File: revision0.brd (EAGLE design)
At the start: 80 x 80 mm, 92 parts, among them IC1 MSP430FR698X(1)80-PIN_PN, IC3 FT232RL

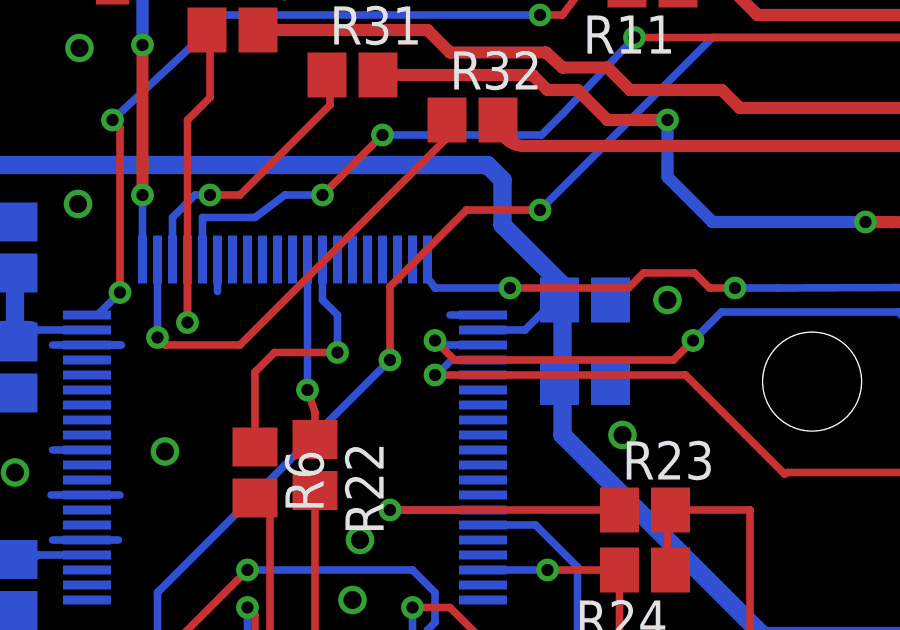
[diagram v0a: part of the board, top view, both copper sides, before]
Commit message: Turn on polygon thermals and fix one GND wire
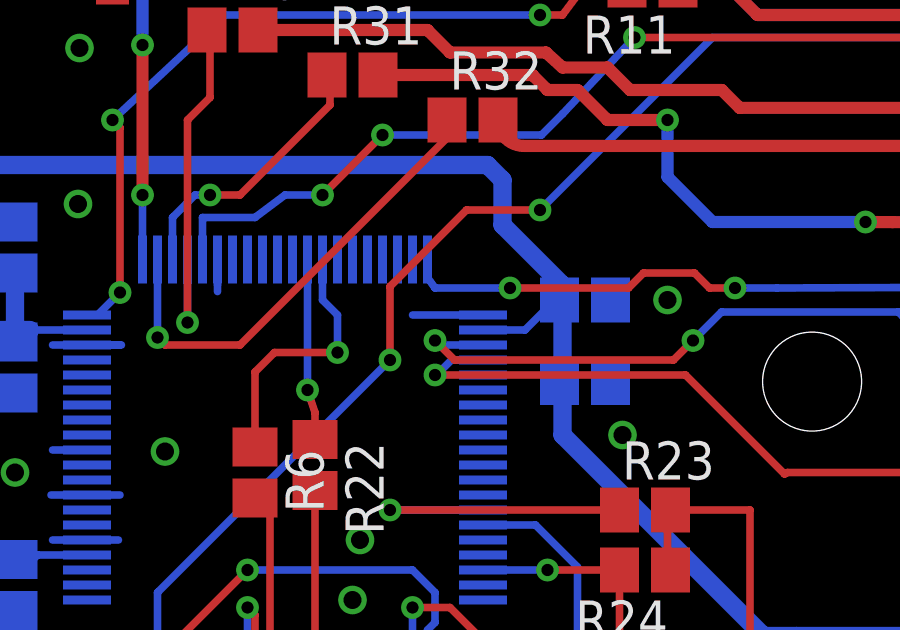
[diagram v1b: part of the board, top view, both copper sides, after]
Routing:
- net GND: track 39.8 -> 41.1 mm
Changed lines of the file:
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@@
 <wire x1="28" y1="71.075" x2="28" y2="71" width="0.4064" layer="1"/>
 <via x="28" y="71" extent="1-16" drill="0.4064"/>
-<polygon width="0.4064" layer="1" thermals="no">
+<polygon width="0.4064" layer="1">
 <vertex x="0.25" y="79.75"/>
 <vertex x="79.75" y="79.75"/>
@@
 <via x="9.25" y="77" extent="1-16" drill="0.6"/>
 <via x="11.75" y="70.75" extent="1-16" drill="0.6"/>
-<polygon width="0.4064" layer="16" thermals="no">
+<polygon width="0.4064" layer="16">
 <vertex x="0.25" y="79.75"/>
 <vertex x="79.75" y="79.75"/>
@@
 <wire x1="33.5" y1="8.5" x2="33.5" y2="11.25" width="0.6096" layer="16"/>
 <wire x1="33.5" y1="11.25" x2="37.5" y2="15.25" width="0.6096" layer="16"/>
-<wire x1="19.5" y1="52" x2="18.25" y2="52" width="0.254" layer="16"/>
+<wire x1="19.5" y1="52" x2="19.35" y2="52" width="0.254" layer="16"/>
 <wire x1="6.25" y1="46" x2="7.25" y2="46" width="0.254" layer="16"/>
 <wire x1="6.15" y1="44.5" x2="7.2" y2="44.5" width="0.254" layer="16"/>
@@
 <via x="8.2" y="68.7" extent="1-16" drill="0.6"/>
 <via x="5.9" y="60.9" extent="1-16" drill="0.6"/>
+<wire x1="19.35" y1="52" x2="17" y2="52" width="0.254" layer="16"/>
 </signal>
 <signal name="GPS-WAKEUP">

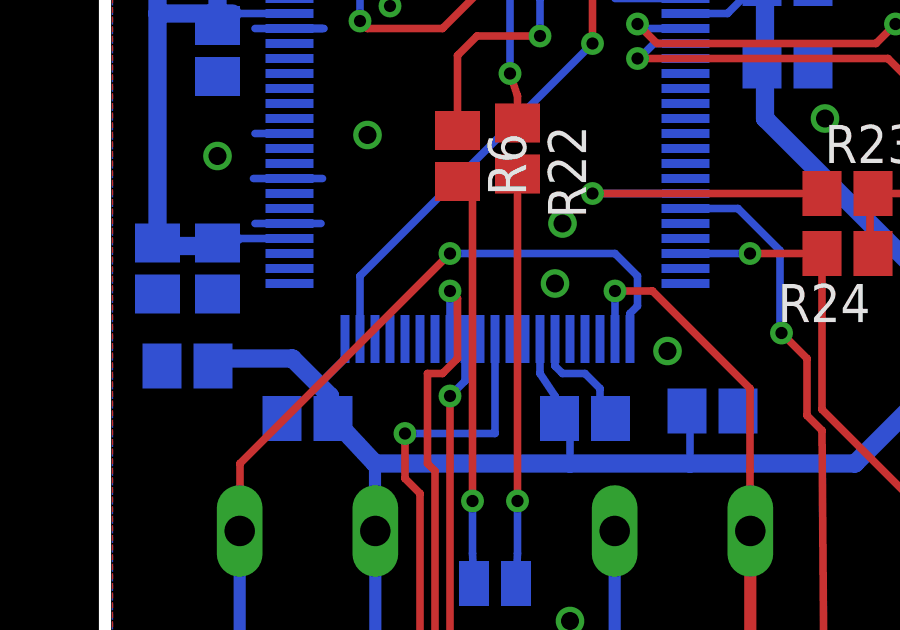
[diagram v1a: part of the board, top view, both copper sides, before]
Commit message: Move GPS-TIMEPULSE sig to interrupt capable input (P2.1)
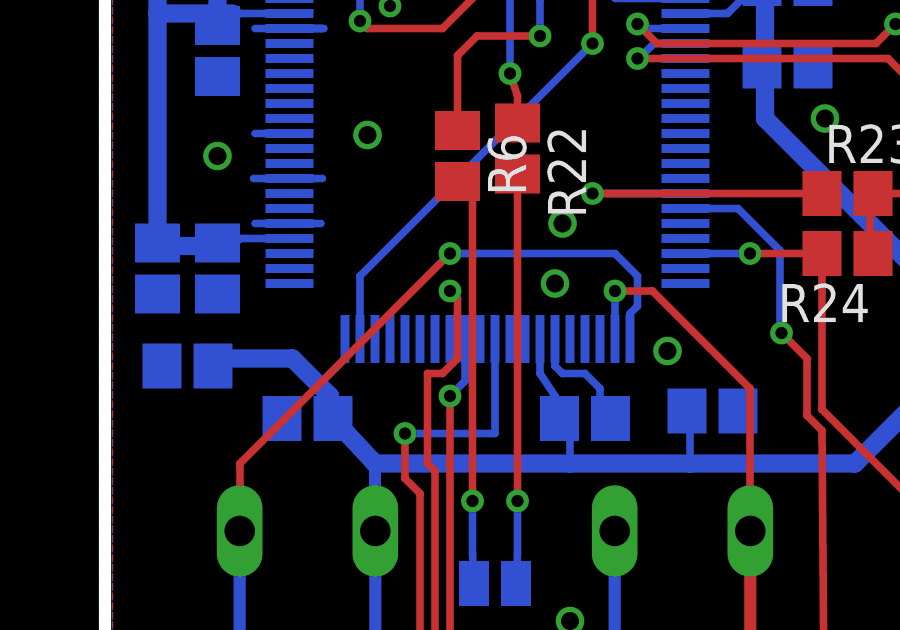
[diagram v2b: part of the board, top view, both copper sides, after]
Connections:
- net GPS-TIMEPULSE: now also IC1.40; no longer IC1.53
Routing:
- net GPS-TIMEPULSE: track 33.2 -> 31.6 mm
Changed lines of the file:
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@@
 <layer number="21" name="tPlace" color="7" fill="1" visible="no" active="yes"/>
 <layer number="22" name="bPlace" color="7" fill="1" visible="no" active="yes"/>
-<layer number="23" name="tOrigins" color="15" fill="1" visible="no" active="yes"/>
-<layer number="24" name="bOrigins" color="15" fill="1" visible="no" active="yes"/>
+<layer number="23" name="tOrigins" color="15" fill="1" visible="yes" active="yes"/>
+<layer number="24" name="bOrigins" color="15" fill="1" visible="yes" active="yes"/>
 <layer number="25" name="tNames" color="7" fill="1" visible="no" active="yes"/>
 <layer number="26" name="bNames" color="7" fill="1" visible="no" active="yes"/>
@@
 <signal name="GPS-TIMEPULSE">
 <contactref element="R28" pad="1"/>
-<contactref element="IC1" pad="53"/>
-<wire x1="11.5" y1="40.65" x2="11.5" y2="42.25" width="0.254" layer="16"/>
 <via x="11.5" y="42.25" extent="1-16" drill="0.4064"/>
 <wire x1="11.75" y1="40" x2="11.25" y2="39.5" width="0.254" layer="1"/>
@@
 <via x="16.5" y="18.95" extent="1-16" drill="0.4064"/>
 <wire x1="16.5" y1="18.95" x2="16.5" y2="13.85" width="0.254" layer="16"/>
+<contactref element="IC1" pad="40"/>
+<wire x1="11.75" y1="42" x2="19.35" y2="42.5" width="0" layer="19" extent="1-16"/>
 </signal>
 <signal name="N$3">

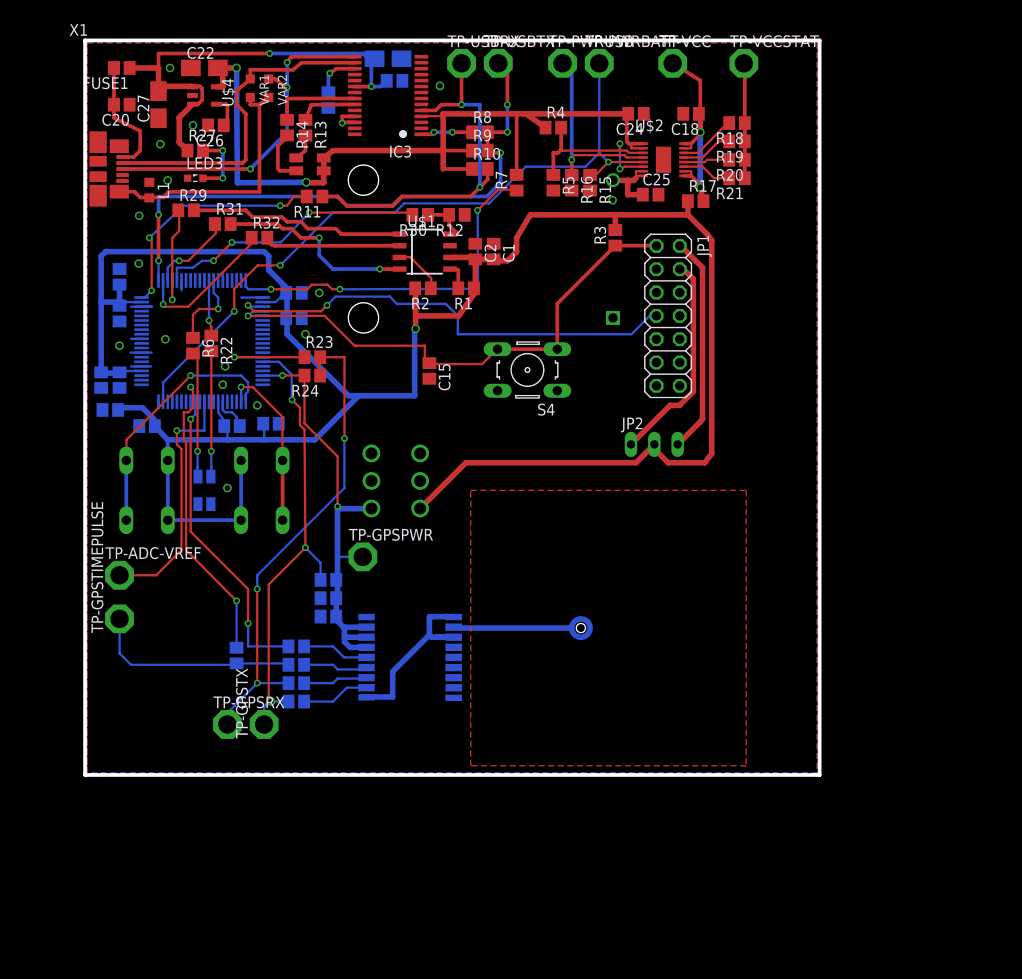
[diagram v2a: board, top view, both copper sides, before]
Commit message: Redesign a lot GPS RF part, CPU pins
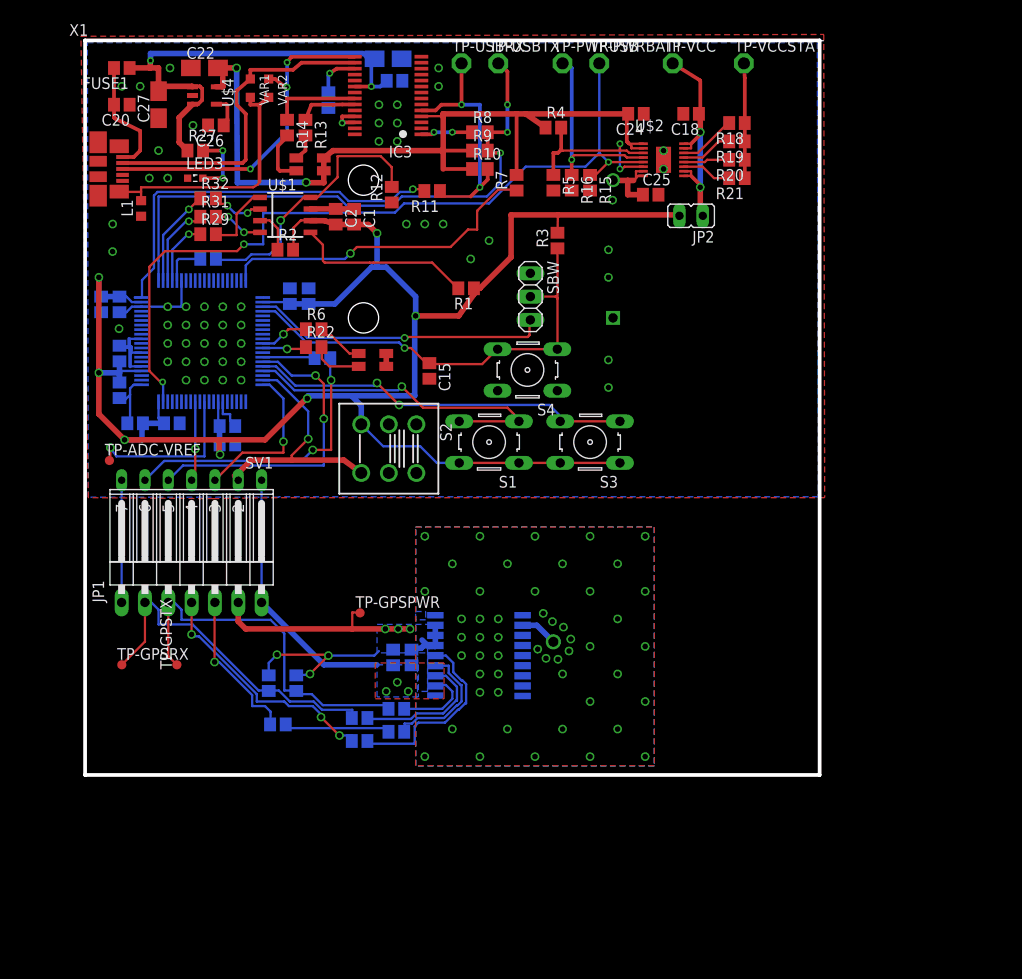
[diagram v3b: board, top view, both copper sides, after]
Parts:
- removed R17: 0, tagps:R0805
- removed TP-GPSTIMEPULSE: TPSQPAD1-20, tagps:P1-20
- added SBW: (no value), tagps:1X03
- added SV1: (no value), tagps:FE07W
- added TP1: TPSQTP16R, tagps:TP16R
- JP1: value JTAG -> (none); device tagps:2X07 -> tagps:1X07/90
- JP2: device tagps:JP2 -> tagps:JP1
- TP-ADC-VREF, TP-GPSPWR, TP-GPSRX, TP-GPSTX: value TPSQPAD1-20 -> TPSQTP10R; device tagps:P1-20 -> tagps:TP10R
- TP-PWRBATT, TP-PWRUSB, TP-USBRX, TP-USBTX, TP-VCC, TP-VCCSTAT: value TPSQPAD1-20 -> TPSQPAD1-13; device tagps:P1-20 -> tagps:P1-13
- moved JP1 58.7 mm to (11.6, 22.6), turned to 0 degrees
- moved S3 48.5 mm to (55.0, 36.2), flipped to the top, turned to 180 degrees
- moved R24 33.8 mm to (20.0, 10.0), flipped to the bottom, turned to 90 degrees
- moved S1 25.3 mm to (44.0, 36.2), flipped to the top, turned to 180 degrees
- moved JP2 25.2 mm to (66.0, 60.9), turned to 90 degrees
- moved R30 23.6 mm to (13.4, 56.2), flipped to the bottom, turned to 0 degrees
- moved LED1 23.2 mm to (31.3, 45.2), flipped to the top, turned to 180 degrees
- moved U$1 15.7 mm to (21.8, 61.0)
- moved C1 15.7 mm to (29.3, 60.8)
- moved C2 15.7 mm to (27.3, 60.8)
- moved R2 15.6 mm to (21.8, 57.2), turned to 0 degrees
- moved R6 13.3 mm to (24.9, 48.5), turned to 0 degrees
- moved TP-GPSRX 13.2 mm to (4.00, 12.0)
- moved FB3 13.1 mm to (33.9, 4.70)
- moved R11 12.8 mm to (37.8, 63.6)
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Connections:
- removed net VCC_TARGET: JP1.4, JP2.1
- removed net VCC_TOOL: JP1.2, JP2.3
- new net MB-GPS-RX: R23.2, SV1.6
- new net MB-GPS-TIMEPULSE: IC1.40, SV1.3
- new net MB-GPS-TX: IC1.35, SV1.5
- new net MB-GPS-WAKEUP: IC1.52, SV1.4
- new net MB_PWR_GPS_SENSE: IC1.39, S2.3.1, SV1.2
- net ANTENNA: now also TP1.TP
- net GND: now also JP1.1, JP1.7, SBW.1, SV1.1, SV1.7; no longer JP1.9
- net GPS-RX: now also JP1.2; no longer R23.2
- net GPS-TIMEPULSE: now also JP1.5; no longer IC1.40
- net GPS-TX: now also JP1.3; no longer IC1.35
- net GPS-WAKEUP: now also JP1.4; no longer IC1.52
- net LED1: now also IC1.32; no longer IC1.12
- net LED2: now also IC1.31; no longer IC1.13
- net N$26: now also JP2.1; no longer R17.2
- net N$9: no longer TP-GPSTIMEPULSE.TP
- net PWR_GPS_SENSE: now also JP1.6; no longer IC1.38, S2.3.1
- net SBW-TCK: now also SBW.3; no longer JP1.7
- net SBW-TDO/TDI: now also SBW.2; no longer JP1.1
- net SW-CFG-GPS: now also IC1.37; no longer IC1.42
- net SW-CHECK-BATT-MEM: now also IC1.36; no longer IC1.41
- net VCC: no longer R17.1
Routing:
- net VCC: track 255.5 -> 202.9 mm, vias 1 -> 7
- net GND: track 41.1 -> 81.2 mm, vias 17 -> 109
- net MB-GPS-TX: track 0.00 -> 34.1 mm, vias 0 -> 2
- net MB-GPS-RX: track 0.00 -> 31.7 mm, vias 0 -> 2
- net MB_PWR_GPS_SENSE: track 0.00 -> 28.5 mm, vias 0 -> 1
- net SPISO: track 30.0 -> 4.78 mm, vias 3 -> 0
- net N$14: track 5.44 -> 29.5 mm, vias 0 -> 1
- net VCC_TOOL: track 23.8 -> 0.00 mm
- net VCC_TARGET: track 23.3 -> 0.00 mm
- net SW-CFG-GPS: track 18.7 -> 37.2 mm
- net SBW-TCK: track 50.8 -> 32.6 mm, vias 2 -> 1
- net MB-GPS-TIMEPULSE: track 0.00 -> 17.5 mm, vias 0 -> 1
- net N$2: track 26.3 -> 43.2 mm, vias 3 -> 1
- net N$11: track 2.94 -> 19.6 mm
- net GPS-RX: track 53.5 -> 37.2 mm, vias 3 -> 0
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- added copper zone on layer 16, net N$4
- added copper zone on layer 16, net PWR_GPS_SENSE
- removed copper zone on layer 1, net N$45
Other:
- board text added: "TIMEPULSE"
- board text removed: "GPS-PULSE"

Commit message: Patch antenna module done
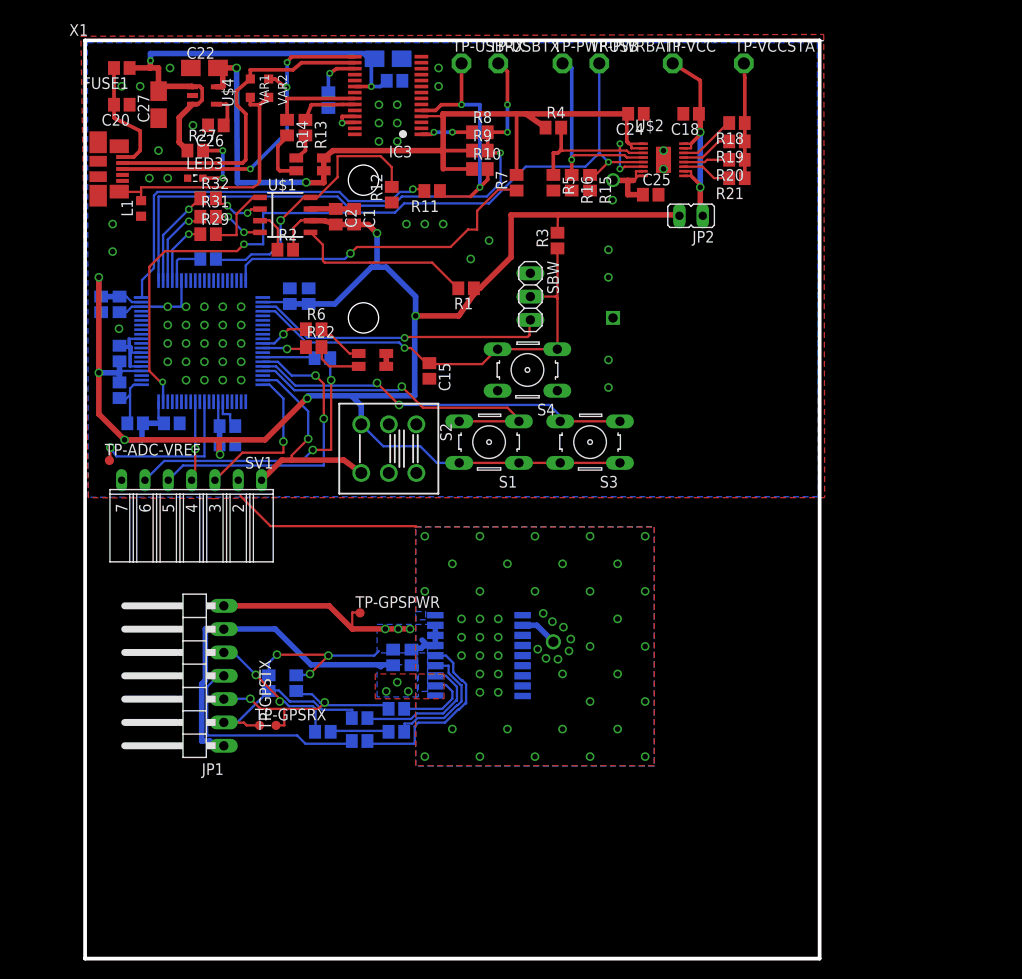
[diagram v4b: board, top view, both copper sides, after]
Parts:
- moved TP-GPSRX 16.4 mm to (19.0, 5.40)
- moved TP-GPSTX 12.7 mm to (20.8, 5.40)
- moved JP1 11.8 mm to (11.3, 10.8), turned to 90 degrees
- moved R28 4.96 mm to (25.9, 4.70)
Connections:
- net GND: now also JP1.6, SV1.2; no longer JP1.7, SV1.1
- net MB_PWR_GPS_SENSE: now also SV1.1; no longer SV1.2
- net PWR_GPS_SENSE: now also JP1.7; no longer JP1.6
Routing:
- net GPS-RX: track 37.2 -> 21.3 mm
- net GND: track 81.2 -> 96.9 mm
- net GPS-TX: track 40.6 -> 26.1 mm, vias 0 -> 2
- net N$9: track 12.1 -> 6.95 mm
- net MB_PWR_GPS_SENSE: track 28.5 -> 24.6 mm
- net GPS-WAKEUP: track 26.9 -> 24.1 mm, vias 3 -> 0
- net GPS-TIMEPULSE: track 17.0 -> 15.3 mm, vias 1 -> 2
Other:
- board size 80 x 80 mm -> 80 x 100 mm
